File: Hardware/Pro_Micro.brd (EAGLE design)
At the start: 17.8 x 33 mm, 33 parts, among them U2 MIC5219, U3 ATMEGA32U4, Y1 16MHz

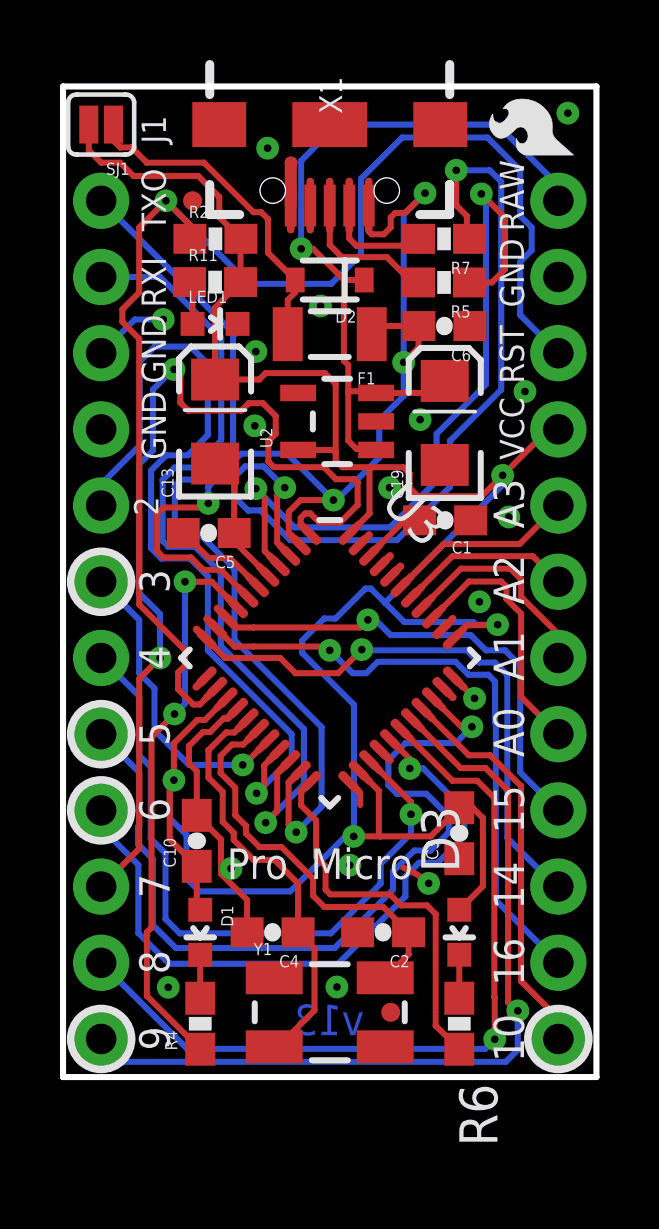
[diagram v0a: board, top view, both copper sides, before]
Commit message: Updated to current library parts with correct labels.  Changed silk to vector font. Moved a few bits of silk to not be over vias. Aligned angled traces to 45 degrees
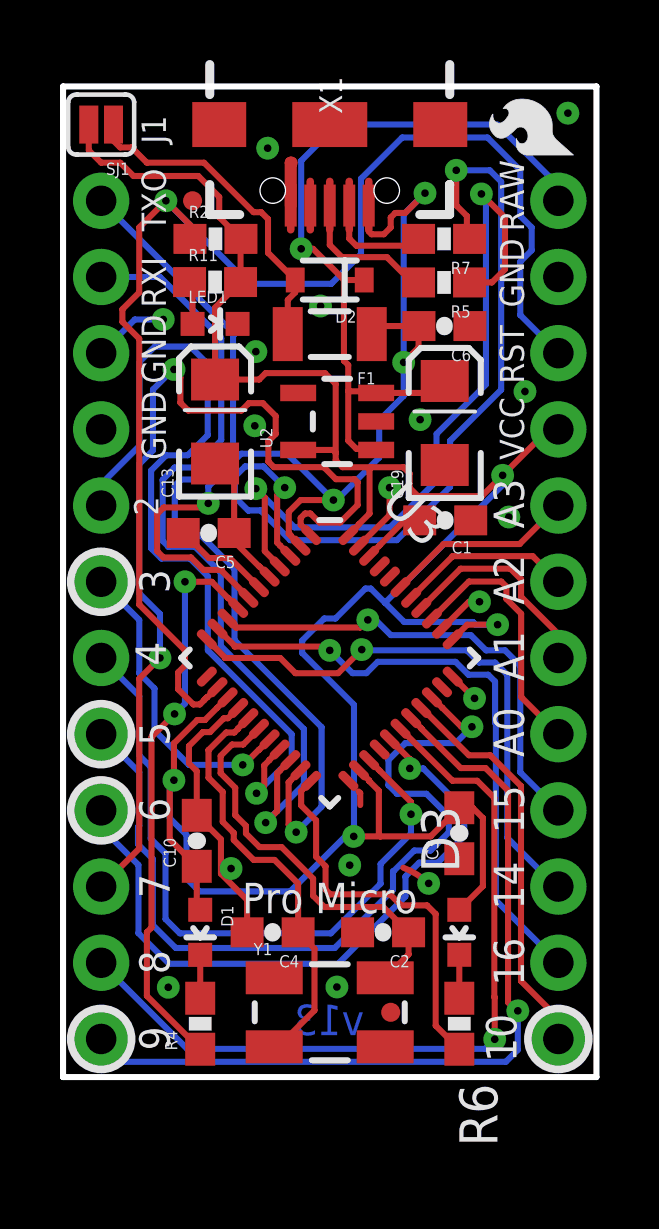
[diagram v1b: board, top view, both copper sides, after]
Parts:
- U3: device Testing:QFN-44-NOPAD_1:1-OUTFAKES -> SparkFun-DigitalIC:QFN-44-NOPAD_1:1-LESS_PASTE
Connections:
- net D14 renamed D17
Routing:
- net GND: track 20.0 -> 24.9 mm
- net VCC: track 83.7 -> 85.2 mm
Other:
- board text added: "Pro Micro"
- board text removed: "Micro"
- board text removed: "Pro"
